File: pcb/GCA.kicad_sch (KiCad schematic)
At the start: 18 parts, among them J2 Conn_01x05_Pin, SW2 SW_SPDT, U1 AT24CM02-SSHM

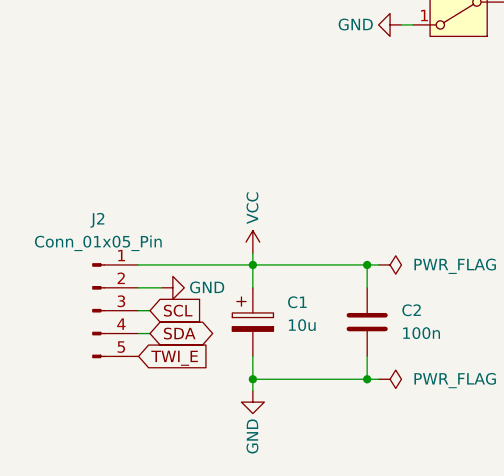
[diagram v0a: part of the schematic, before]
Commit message: Flip connector to top
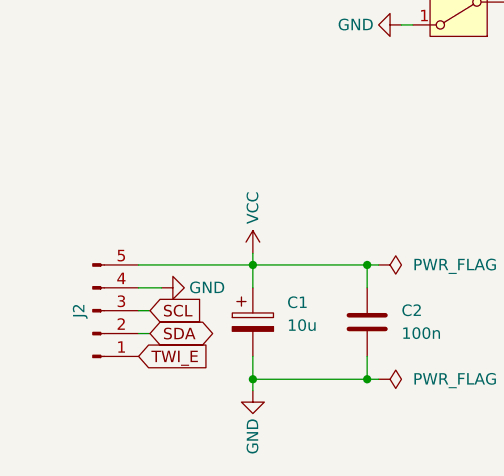
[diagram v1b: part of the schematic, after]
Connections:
- net GND: now also J2.4 (Pin_4); no longer J2.2 (Pin_2)
- net SDA: now also J2.2 (Pin_2); no longer J2.4 (Pin_4)
- net TWI_E: now also J2.1 (Pin_1); no longer J2.5 (Pin_5)
- net VCC: now also J2.5 (Pin_5); no longer J2.1 (Pin_1)
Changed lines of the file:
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@@
 		(lib_id "Connector:Conn_01x05_Pin")
 		(at 54.61 138.43 0)
+		(mirror x)
 		(unit 1)
 		(exclude_from_sim no)
@@
 		(on_board yes)
 		(dnp no)
-		(fields_autoplaced yes)
 		(property "Reference" "J2"
-			(at 55.245 128.27 0)
+			(at 53.086 138.43 90)
 			(effects
 				(font
@@
 		)
 		(property "Value" "Conn_01x05_Pin"
-			(at 55.245 130.81 0)
+			(at 55.245 146.05 0)
 			(effects
 				(font
 					(size 1.27 1.27)
 				)
+				(hide yes)
 			)
 		)
